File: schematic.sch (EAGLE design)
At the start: 13 parts, among them Q1 DTC114EM3T5G, U1 2-1393222-0, U2 TLP627-2, U3 ATTINY85-20SU, U4 TLP627-2, X1 C-05843_USB-MINI-B32005-201

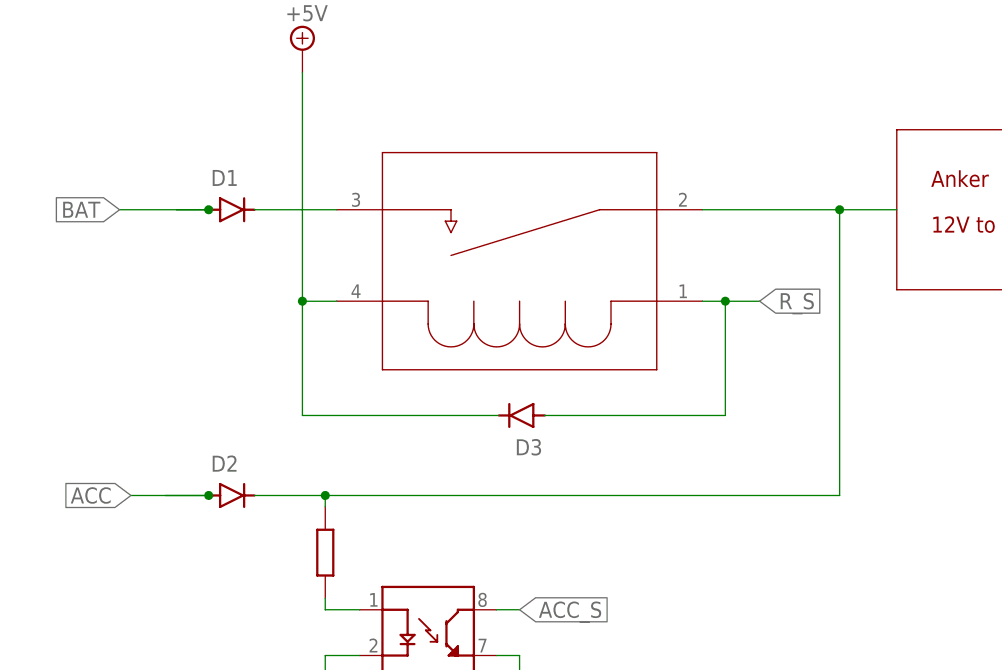
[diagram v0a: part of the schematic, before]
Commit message: ダイオードの位置修正
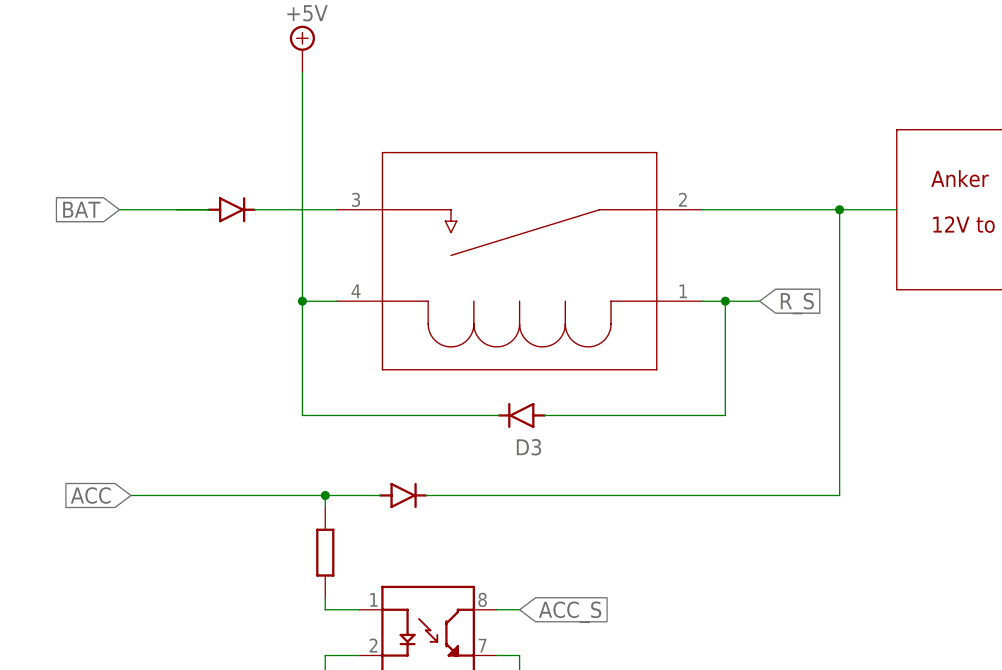
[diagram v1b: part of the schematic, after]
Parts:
- removed D2: 1N4004, Diodes:1N4004
- added D4: 1N4004, Diodes:1N4004
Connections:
- removed net N$2: D2.C, R1.2, U1.2
- net ACC: now also D4.A, D4.C, R1.2, U1.2; no longer D2.A
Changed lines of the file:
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@@
 <part name="D1" library="Diodes" library_urn="urn:adsk.eagle:library:11396254" deviceset="1N4004" device="" package3d_urn="urn:adsk.eagle:package:10898391/4"/>
 <part name="FRAME1" library="frames" library_urn="urn:adsk.eagle:library:229" deviceset="A4L-LOC" device=""/>
-<part name="D2" library="Diodes" library_urn="urn:adsk.eagle:library:11396254" deviceset="1N4004" device="" package3d_urn="urn:adsk.eagle:package:10898391/4"/>
 <part name="U1" library="Relays" library_urn="urn:adsk.eagle:library:14869337" deviceset="2-1393222-0" device="" package3d_urn="urn:adsk.eagle:package:14869499/2"/>
 <part name="SUPPLY1" library="supply2" library_urn="urn:adsk.eagle:library:372" deviceset="+5V" device=""/>
@@
 <part name="Q1" library="DTC114E" deviceset="DTC114E" device="M3T5G"/>
 <part name="GND7" library="supply1" library_urn="urn:adsk.eagle:library:371" deviceset="GND" device=""/>
+<part name="D4" library="Diodes" library_urn="urn:adsk.eagle:library:11396254" deviceset="1N4004" device="" package3d_urn="urn:adsk.eagle:package:10898391/4"/>
 </parts>
 <sheets>
@@
 </plain>
 <instances>
-<instance part="D1" gate="G$1" x="41.656" y="142.24" smashed="yes">
-<attribute name="NAME" x="39.3446" y="144.8816" size="1.778" layer="95"/>
-</instance>
+<instance part="D1" gate="G$1" x="41.656" y="142.24" smashed="yes"/>
 <instance part="FRAME1" gate="G$1" x="0" y="0" smashed="yes">
 <attribute name="DRAWING_NAME" x="215.646" y="14.986" size="1.4224" layer="94" font="vector"/>
 <attribute name="LAST_DATE_TIME" x="217.17" y="10.16" size="2.286" layer="94"/>
 <attribute name="SHEET" x="230.505" y="5.08" size="2.54" layer="94"/>
-</instance>
-<instance part="D2" gate="G$1" x="41.656" y="110.49" smashed="yes">
-<attribute name="NAME" x="39.3446" y="113.1316" size="1.778" layer="95"/>
 </instance>
 <instance part="U1" gate="A" x="73.66" y="137.16" smashed="yes" rot="R180"/>
@@
 </instance>
 <instance part="GND7" gate="1" x="93.98" y="39.37" smashed="yes"/>
+<instance part="D4" gate="G$1" x="60.706" y="110.49" smashed="yes"/>
 </instances>
 <busses>
@@
 <pinref part="D1" gate="G$1" pin="A"/>
 <wire x1="39.116" y1="142.24" x2="29.21" y2="142.24" width="0.1524" layer="91"/>
-<junction x="39.116" y="142.24"/>
 </segment>
 </net>
 <net name="ACC" class="0">
 <segment>
-<wire x1="34.29" y1="110.49" x2="39.116" y2="110.49" width="0.1524" layer="91"/>
+<wire x1="63.246" y1="110.49" x2="109.22" y2="110.49" width="0.1524" layer="91"/>
+<wire x1="109.22" y1="110.49" x2="109.22" y2="142.24" width="0.1524" layer="91"/>
+<wire x1="109.22" y1="142.24" x2="93.98" y2="142.24" width="0.1524" layer="91"/>
+<pinref part="U1" gate="A" pin="2"/>
+<wire x1="109.22" y1="142.24" x2="115.57" y2="142.24" width="0.1524" layer="91"/>
+<junction x="109.22" y="142.24"/>
+<pinref part="D4" gate="G$1" pin="C"/>
+</segment>
+<segment>
+<pinref part="R1" gate="G$1" pin="2"/>
+<wire x1="52.07" y1="109.22" x2="52.07" y2="110.49" width="0.1524" layer="91"/>
+<wire x1="52.07" y1="110.49" x2="30.48" y2="110.49" width="0.1524" layer="91"/>
 <label x="30.48" y="110.49" size="1.778" layer="95" rot="R180" xref="yes"/>
-<pinref part="D2" gate="G$1" pin="A"/>
-<wire x1="39.116" y1="110.49" x2="30.48" y2="110.49" width="0.1524" layer="91"/>
-<junction x="39.116" y="110.49"/>
+<pinref part="D4" gate="G$1" pin="A"/>
+<wire x1="58.166" y1="110.49" x2="52.07" y2="110.49" width="0.1524" layer="91"/>
+<junction x="52.07" y="110.49"/>
 </segment>
 </net>
@@
 </segment>
 </net>
-<net name="N$2" class="0">
-<segment>
-<pinref part="D2" gate="G$1" pin="C"/>
-<wire x1="44.196" y1="110.49" x2="52.07" y2="110.49" width="0.1524" layer="91"/>
-<wire x1="52.07" y1="110.49" x2="109.22" y2="110.49" width="0.1524" layer="91"/>
-<wire x1="109.22" y1="110.49" x2="109.22" y2="142.24" width="0.1524" layer="91"/>
-<wire x1="109.22" y1="142.24" x2="93.98" y2="142.24" width="0.1524" layer="91"/>
-<pinref part="U1" gate="A" pin="2"/>
-<pinref part="R1" gate="G$1" pin="2"/>
-<wire x1="52.07" y1="109.22" x2="52.07" y2="110.49" width="0.1524" layer="91"/>
-<junction x="52.07" y="110.49"/>
-<wire x1="109.22" y1="142.24" x2="115.57" y2="142.24" width="0.1524" layer="91"/>
-<junction x="109.22" y="142.24"/>
-</segment>
-</net>
